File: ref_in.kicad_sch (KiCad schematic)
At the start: 15 parts, among them U1101 74LVC2GU04, U1102 74LVC2G04

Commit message: Update footprints: - SOD323F, SOD323, SOD123W... intead of generic handsolder version - 3225 xtal - use handsolder footprint - do not use handsolder version for ferrite beads - use SOT-23-6 instead of TSOP-6
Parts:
- D1102, D1103: footprint Diode_SMD:D_SOD-323_HandSoldering -> Diode_SMD:D_SOD-323F
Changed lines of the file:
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@@
       (effects (font (size 1.27 1.27)) (justify left))
     )
-    (property "Footprint" "Diode_SMD:D_SOD-323_HandSoldering" (id 2) (at 126.365 96.52 0)
+    (property "Footprint" "Diode_SMD:D_SOD-323F" (id 2) (at 126.365 96.52 0)
       (effects (font (size 1.27 1.27)) hide)
     )
@@
       (effects (font (size 1.27 1.27)) (justify left))
     )
-    (property "Footprint" "Diode_SMD:D_SOD-323_HandSoldering" (id 2) (at 125.095 106.68 0)
-      (effects (font (size 1.27 1.27)) hide)
-    )
+    (property "Footprint" "Diode_SMD:D_SOD-323F" (id 2) (at 125.095 106.68 0)
+      (effects (font (size 1.27 1.27)) hide)
+    )

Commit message: 74lvc2g04: swap units
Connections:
- net OUT: now also U1102.6; no longer U1102.4
- net at U1101.4: now also U1102.3; no longer U1102.1
- new net: U1102.1, U1102.4
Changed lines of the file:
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@@
     (pin "2")
   )
-  (symbol (lib_id "symbols:74LVC2G04") (at 189.23 101.6 0) (unit 1)
+  (symbol (lib_id "symbols:74LVC2G04") (at 189.23 101.6 0) (unit 2)
     (in_bom yes) (on_board yes) (fields_autoplaced)
     (property "Reference" "U1102" (id 0) (at 191.0715 94.0902 0))
@@
     (pin "5")
   )
-  (symbol (lib_id "symbols:74LVC2G04") (at 205.74 101.6 0) (unit 2)
+  (symbol (lib_id "symbols:74LVC2G04") (at 205.74 101.6 0) (unit 1)
     (in_bom yes) (on_board yes) (fields_autoplaced)
     (property "Reference" "U1102" (id 0) (at 207.5815 94.0902 0))

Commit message: Reconnect some things to simplify PCB routing
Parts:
- U1101: value 74LVC2GU04 -> (none); footprint Package_TO_SOT_SMD:SOT-23-6 -> (none)
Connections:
- net IN: now also C1102.1, JP1101.1 (A); no longer R1102.2
- net at D1102.1 (K), D1103.2 (A), R1103.1: now also R1102.1, U1101.3; no longer C1102.2, JP1101.2 (B), U1101.1
- net at U1102.3: now also U1101.6; no longer U1101.4
- new net: C1102.2, JP1101.2 (B), R1102.2
- new net: R1104.1, U1101.1, U1101.4
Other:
- moved on the sheet: C1102, JP1101, R1102
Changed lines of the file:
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@@
   (junction (at 147.32 113.03) (diameter 0) (color 0 0 0 0)
   )
+  (junction (at 129.54 101.6) (diameter 0) (color 0 0 0 0)
+  )
   (junction (at 203.2 60.96) (diameter 0) (color 0 0 0 0)
   )
-  (junction (at 129.54 101.6) (diameter 0) (color 0 0 0 0)
-  )
   (junction (at 73.66 101.6) (diameter 0) (color 0 0 0 0)
   )
@@
   (junction (at 165.1 50.8) (diameter 0) (color 0 0 0 0)
   )
+  (junction (at 111.76 101.6) (diameter 0) (color 0 0 0 0)
+  )
   (junction (at 165.1 60.96) (diameter 0) (color 0 0 0 0)
   )
-  (junction (at 110.49 101.6) (diameter 0) (color 0 0 0 0)
+  (junction (at 99.06 101.6) (diameter 0) (color 0 0 0 0)
   )
   (junction (at 203.2 50.8) (diameter 0) (color 0 0 0 0)
@@
   (junction (at 147.32 101.6) (diameter 0) (color 0 0 0 0)
   )
-  (junction (at 123.19 101.6) (diameter 0) (color 0 0 0 0)
-  )
   (junction (at 184.15 50.8) (diameter 0) (color 0 0 0 0)
   )
@@
     (stroke (width 0) (type default) (color 0 0 0 0))
   )
-  (wire (pts (xy 123.19 101.6) (xy 129.54 101.6))
-    (stroke (width 0) (type default) (color 0 0 0 0))
-  )
   (wire (pts (xy 215.9 60.96) (xy 203.2 60.96))
     (stroke (width 0) (type default) (color 0 0 0 0))
@@
     (stroke (width 0) (type default) (color 0 0 0 0))
   )
-  (wire (pts (xy 123.19 91.44) (xy 123.19 101.6))
+  (wire (pts (xy 111.76 91.44) (xy 111.76 101.6))
     (stroke (width 0) (type default) (color 0 0 0 0))
   )
@@
     (stroke (width 0) (type default) (color 0 0 0 0))
   )
-  (wire (pts (xy 106.68 101.6) (xy 110.49 101.6))
-    (stroke (width 0) (type default) (color 0 0 0 0))
-  )
   (wire (pts (xy 147.32 110.49) (xy 147.32 113.03))
     (stroke (width 0) (type default) (color 0 0 0 0))
   )
-  (wire (pts (xy 110.49 101.6) (xy 113.03 101.6))
+  (wire (pts (xy 99.06 101.6) (xy 101.6 101.6))
     (stroke (width 0) (type default) (color 0 0 0 0))
   )
@@
     (stroke (width 0) (type default) (color 0 0 0 0))
   )
+  (wire (pts (xy 124.46 101.6) (xy 129.54 101.6))
+    (stroke (width 0) (type default) (color 0 0 0 0))
+  )
+  (wire (pts (xy 111.76 101.6) (xy 116.84 101.6))
+    (stroke (width 0) (type default) (color 0 0 0 0))
+  )
   (wire (pts (xy 184.15 60.96) (xy 165.1 60.96))
     (stroke (width 0) (type default) (color 0 0 0 0))
   )
-  (wire (pts (xy 110.49 91.44) (xy 110.49 101.6))
+  (wire (pts (xy 99.06 91.44) (xy 99.06 101.6))
     (stroke (width 0) (type default) (color 0 0 0 0))
   )
@@
     (stroke (width 0) (type default) (color 0 0 0 0))
   )
-  (wire (pts (xy 121.92 91.44) (xy 123.19 91.44))
+  (wire (pts (xy 110.49 91.44) (xy 111.76 91.44))
     (stroke (width 0) (type default) (color 0 0 0 0))
   )
@@
     (stroke (width 0) (type default) (color 0 0 0 0))
   )
-  (wire (pts (xy 111.76 91.44) (xy 110.49 91.44))
-    (stroke (width 0) (type default) (color 0 0 0 0))
-  )
-  (wire (pts (xy 120.65 101.6) (xy 123.19 101.6))
+  (wire (pts (xy 100.33 91.44) (xy 99.06 91.44))
+    (stroke (width 0) (type default) (color 0 0 0 0))
+  )
+  (wire (pts (xy 109.22 101.6) (xy 111.76 101.6))
     (stroke (width 0) (type default) (color 0 0 0 0))
   )
@@
     (pin "3")
   )
-  (symbol (lib_id "Device:C") (at 116.84 101.6 90) (unit 1)
-    (in_bom yes) (on_board yes) (fields_autoplaced)
-    (property "Reference" "C1102" (id 0) (at 116.84 105.7894 90))
-    (property "Value" "10n" (id 1) (at 116.84 108.3263 90))
-    (property "Footprint" "Capacitor_SMD:C_0805_2012Metric" (id 2) (at 120.65 100.6348 0)
-      (effects (font (size 1.27 1.27)) hide)
-    )
-    (property "Datasheet" "~" (id 3) (at 116.84 101.6 0)
-      (effects (font (size 1.27 1.27)) hide)
-    )
-    (property "Spec1" "" (id 4) (at 116.84 110.8632 90))
-    (property "Spec2" "C0G" (id 5) (at 116.84 110.8632 90))
-    (property "Tolerance" "" (id 6) (at 116.84 115.937 90))
-    (property "Mfr" "Murata" (id 7) (at 116.84 101.6 0)
-      (effects (font (size 1.27 1.27)) hide)
-    )
-    (property "Mfr PN" "GRM2165C2A103JA01" (id 8) (at 116.84 101.6 0)
+  (symbol (lib_id "Device:C") (at 105.41 101.6 90) (unit 1)
+    (in_bom yes) (on_board yes) (fields_autoplaced)
+    (property "Reference" "C1102" (id 0) (at 105.41 105.7894 90))
+    (property "Value" "10n" (id 1) (at 105.41 108.3263 90))
+    (property "Footprint" "Capacitor_SMD:C_0805_2012Metric" (id 2) (at 109.22 100.6348 0)
+      (effects (font (size 1.27 1.27)) hide)
+    )
+    (property "Datasheet" "~" (id 3) (at 105.41 101.6 0)
+      (effects (font (size 1.27 1.27)) hide)
+    )
+    (property "Spec1" "" (id 4) (at 105.41 110.8632 90))
+    (property "Spec2" "C0G" (id 5) (at 105.41 110.8632 90))
+    (property "Tolerance" "" (id 6) (at 105.41 115.937 90))
+    (property "Mfr" "Murata" (id 7) (at 105.41 101.6 0)
+      (effects (font (size 1.27 1.27)) hide)
+    )
+    (property "Mfr PN" "GRM2165C2A103JA01" (id 8) (at 105.41 101.6 0)
       (effects (font (size 1.27 1.27)) hide)
     )
@@
     (pin "1")
   )
-  (symbol (lib_id "Jumper:Jumper_2_Open") (at 116.84 91.44 0) (unit 1)
-    (in_bom yes) (on_board yes) (fields_autoplaced)
-    (property "Reference" "JP1101" (id 0) (at 116.84 86.0892 0))
-    (property "Value" "DC" (id 1) (at 116.84 88.6261 0))
-    (property "Footprint" "Connector_PinHeader_2.54mm:PinHeader_1x02_P2.54mm_Vertical" (id 2) (at 116.84 91.44 0)
-      (effects (font (size 1.27 1.27)) hide)
-    )
-    (property "Datasheet" "~" (id 3) (at 116.84 91.44 0)
+  (symbol (lib_id "Jumper:Jumper_2_Open") (at 105.41 91.44 0) (unit 1)
+    (in_bom yes) (on_board yes) (fields_autoplaced)
+    (property "Reference" "JP1101" (id 0) (at 105.41 86.0892 0))
+    (property "Value" "DC" (id 1) (at 105.41 88.6261 0))
+    (property "Footprint" "Connector_PinHeader_2.54mm:PinHeader_1x02_P2.54mm_Vertical" (id 2) (at 105.41 91.44 0)
+      (effects (font (size 1.27 1.27)) hide)
+    )
+    (property "Datasheet" "~" (id 3) (at 105.41 91.44 0)
       (effects (font (size 1.27 1.27)) hide)
     )
@@
     (pin "2")
   )
-  (symbol (lib_id "symbols:74LVC2GU04") (at 172.72 101.6 0) (unit 2)
+  (symbol (lib_id "symbols:74LVC2GU04") (at 172.72 101.6 0) (unit 1)
     (in_bom yes) (on_board yes) (fields_autoplaced)
     (property "Reference" "U1101" (id 0) (at 174.5615 94.0902 0))
-    (property "Value" "74LVC2GU04" (id 1) (at 174.5615 96.6271 0))
-    (property "Footprint" "Package_TO_SOT_SMD:SOT-23-6" (id 2) (at 172.72 83.82 0)
+    (property "Value" "" (id 1) (at 174.5615 96.6271 0))
+    (property "Footprint" "" (id 2) (at 172.72 83.82 0)
       (effects (font (size 1.27 1.27)) hide)
     )
@@
       (effects (font (size 1.27 1.27)) (justify left))
     )
-    (property "Value" "74LVC2GU04" (id 1) (at 186.3713 57.5822 0)
-      (effects (font (size 1.27 1.27)) (justify left))
-    )
-    (property "Footprint" "Package_TO_SOT_SMD:SOT-23-6" (id 2) (at 184.15 38.1 0)
+    (property "Value" "" (id 1) (at 186.3713 57.5822 0)
+      (effects (font (size 1.27 1.27)) (justify left))
+    )
+    (property "Footprint" "" (id 2) (at 184.15 38.1 0)
       (effects (font (size 1.27 1.27)) hide)
     )
@@
     (pin "2")
   )
-  (symbol (lib_id "Device:R") (at 102.87 101.6 270) (unit 1)
-    (in_bom yes) (on_board yes) (fields_autoplaced)
-    (property "Reference" "R1102" (id 0) (at 102.87 96.8842 90))
-    (property "Value" "1k" (id 1) (at 102.87 99.4211 90))
-    (property "Footprint" "Resistor_SMD:R_0805_2012Metric" (id 2) (at 102.87 99.822 90)
-      (effects (font (size 1.27 1.27)) hide)
-    )
-    (property "Datasheet" "~" (id 3) (at 102.87 101.6 0)
-      (effects (font (size 1.27 1.27)) hide)
-    )
-    (property "Tolerance" "" (id 4) (at 102.87 101.6 0)
-      (effects (font (size 1.27 1.27)) hide)
-    )
-    (property "Mfr" "Bourns" (id 5) (at 102.87 101.6 0)
-      (effects (font (size 1.27 1.27)) hide)
-    )
-    (property "Mfr PN" "CR0805-FX-1001ELF" (id 6) (at 102.87 101.6 0)
-      (effects (font (size 1.27 1.27)) hide)
-    )
-    (pin "1")
-    (pin "2")
-  )
-  (symbol (lib_id "symbols:74LVC2GU04") (at 154.94 101.6 0) (unit 1)
+  (symbol (lib_id "Device:R") (at 120.65 101.6 270) (unit 1)
+    (in_bom yes) (on_board yes) (fields_autoplaced)
+    (property "Reference" "R1102" (id 0) (at 120.65 96.8842 90))
+    (property "Value" "1k" (id 1) (at 120.65 99.4211 90))
+    (property "Footprint" "Resistor_SMD:R_0805_2012Metric" (id 2) (at 120.65 99.822 90)
+      (effects (font (size 1.27 1.27)) hide)
+    )
+    (property "Datasheet" "~" (id 3) (at 120.65 101.6 0)
+      (effects (font (size 1.27 1.27)) hide)
+    )
+    (property "Tolerance" "" (id 4) (at 120.65 101.6 0)
+      (effects (font (size 1.27 1.27)) hide)
+    )
+    (property "Mfr" "Bourns" (id 5) (at 120.65 101.6 0)
+      (effects (font (size 1.27 1.27)) hide)
+    )
+    (property "Mfr PN" "CR0805-FX-1001ELF" (id 6) (at 120.65 101.6 0)
+      (effects (font (size 1.27 1.27)) hide)
+    )
+    (pin "1")
+    (pin "2")
+  )
+  (symbol (lib_id "symbols:74LVC2GU04") (at 154.94 101.6 0) (unit 2)
     (in_bom yes) (on_board yes) (fields_autoplaced)
     (property "Reference" "U1101" (id 0) (at 156.7815 94.0902 0))
-    (property "Value" "74LVC2GU04" (id 1) (at 156.7815 96.6271 0))
-    (property "Footprint" "Package_TO_SOT_SMD:SOT-23-6" (id 2) (at 154.94 83.82 0)
-      (effects (font (size 1.27 1.27)) hide)
-    )
+    (property "Value" "" (id 1) (at 156.7815 96.6271 0))
+    (property "Footprint" "" (id 2) (at 154.94 83.82 0)
+      (effects (font (size 1.27 1.27)) hide)
+    )

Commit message: Fix footprints, values and PNs
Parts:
- U1101: value (none) -> 74LVC2GU04; footprint (none) -> Package_TO_SOT_SMD:SOT-23-6
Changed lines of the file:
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@@
     (in_bom yes) (on_board yes) (fields_autoplaced)
     (property "Reference" "U1101" (id 0) (at 174.5615 94.0902 0))
-    (property "Value" "" (id 1) (at 174.5615 96.6271 0))
-    (property "Footprint" "" (id 2) (at 172.72 83.82 0)
+    (property "Value" "74LVC2GU04" (id 1) (at 174.5615 96.6271 0))
+    (property "Footprint" "Package_TO_SOT_SMD:SOT-23-6" (id 2) (at 172.72 83.82 0)
       (effects (font (size 1.27 1.27)) hide)
     )
@@
       (effects (font (size 1.27 1.27)) (justify left))
     )
-    (property "Value" "" (id 1) (at 186.3713 57.5822 0)
-      (effects (font (size 1.27 1.27)) (justify left))
-    )
-    (property "Footprint" "" (id 2) (at 184.15 38.1 0)
+    (property "Value" "74LVC2GU04" (id 1) (at 186.3713 57.5822 0)
+      (effects (font (size 1.27 1.27)) (justify left))
+    )
+    (property "Footprint" "Package_TO_SOT_SMD:SOT-23-6" (id 2) (at 184.15 38.1 0)
       (effects (font (size 1.27 1.27)) hide)
     )
@@
     (in_bom yes) (on_board yes) (fields_autoplaced)
     (property "Reference" "U1101" (id 0) (at 156.7815 94.0902 0))
-    (property "Value" "" (id 1) (at 156.7815 96.6271 0))
-    (property "Footprint" "" (id 2) (at 154.94 83.82 0)
-      (effects (font (size 1.27 1.27)) hide)
-    )
+    (property "Value" "74LVC2GU04" (id 1) (at 156.7815 96.6271 0))
+    (property "Footprint" "Package_TO_SOT_SMD:SOT-23-6" (id 2) (at 154.94 83.82 0)
+      (effects (font (size 1.27 1.27)) hide)
+    )

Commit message: VCXO, REF_IN: add reflection damping resistors
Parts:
- added R1105: 49.9, Resistor_SMD:R_0805_2012Metric, symbol Device:R
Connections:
- net OUT: now also R1105.2; no longer U1102.6
- new net: R1105.1, U1102.6
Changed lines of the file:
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@@
     (stroke (width 0) (type default) (color 0 0 0 0))
   )
-  (wire (pts (xy 213.36 101.6) (xy 218.44 101.6))
+  (wire (pts (xy 213.36 101.6) (xy 217.17 101.6))
     (stroke (width 0) (type default) (color 0 0 0 0))
   )
@@
     (stroke (width 0) (type default) (color 0 0 0 0))
   )
+  (wire (pts (xy 224.79 101.6) (xy 228.6 101.6))
+    (stroke (width 0) (type default) (color 0 0 0 0))
+  )
   (wire (pts (xy 203.2 50.8) (xy 203.2 52.07))
     (stroke (width 0) (type default) (color 0 0 0 0))
@@
     (stroke (width 0) (type default) (color 0 0 0 0))
   )
-  (hierarchical_label "OUT" (shape output) (at 218.44 101.6 0)
+  (hierarchical_label "OUT" (shape output) (at 228.6 101.6 0)
     (effects (font (size 1.27 1.27)) (justify left))
   )
@@
       (effects (font (size 1.27 1.27)) hide)
     )
+    (pin "1")
+    (pin "2")
+  )
+  (symbol (lib_id "Device:R") (at 220.98 101.6 90) (unit 1)
+    (in_bom yes) (on_board yes) (fields_autoplaced)
+    (property "Reference" "R1105" (id 0) (at 220.98 96.8842 90))
+    (property "Value" "49.9" (id 1) (at 220.98 99.4211 90))
+    (property "Footprint" "Resistor_SMD:R_0805_2012Metric" (id 2) (at 220.98 103.378 90)
+      (effects (font (size 1.27 1.27)) hide)
+    )
+    (property "Datasheet" "~" (id 3) (at 220.98 101.6 0)
+      (effects (font (size 1.27 1.27)) hide)
+    )
+    (property "Mfr" "Bourns" (id 4) (at 220.98 101.6 0)
+      (effects (font (size 1.27 1.27)) hide)
+    )
+    (property "Mfr PN" "CR0805-FX-49R9ELF" (id 5) (at 220.98 101.6 0)
+      (effects (font (size 1.27 1.27)) hide)
+    )

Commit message: PCB: WIP Schematic: minor changes (decoupling, logic element ordering)
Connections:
- net at D1102.1 (K), D1103.2 (A), R1102.1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: now also U1101.1; no longer U1101.3
- net at R1105.1: now also U1102.4; no longer U1102.6
- net at U1101.6: now also R1104.1, U1101.3; no longer U1102.3
- net at U1102.1: now also U1101.4; no longer U1102.4
- new net: U1102.3, U1102.6
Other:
- moved on the sheet: U1101A, U1101B, U1102A, U1102B

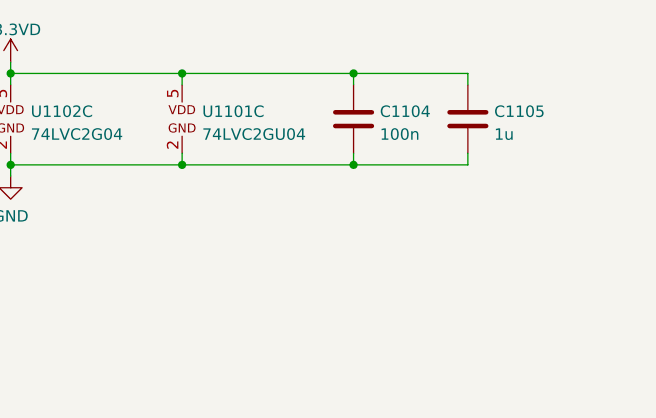
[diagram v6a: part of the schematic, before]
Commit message: Update schematic: - Redesign of decoupling based on swcad modelling (predominantly use 1uf, no paralleled caps) - Reroute REF_CLK_IN, CLK_SEL net to different FPGA pins - Some net renaming - Ext conn: add decoupling to 3v3 output - Reassign references to all components PCB: routing almost finished
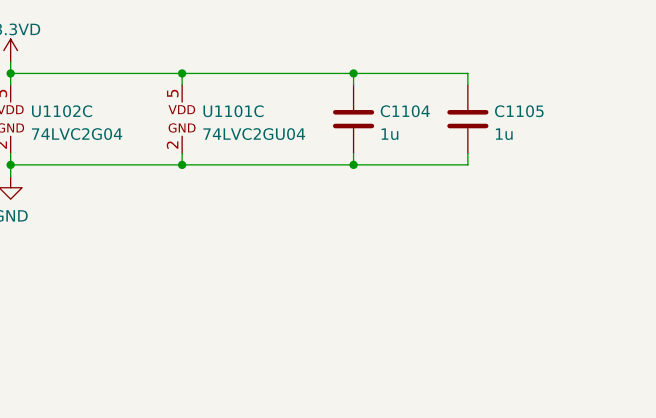
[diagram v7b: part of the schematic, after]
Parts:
- C1104: value 100n -> 1u; Mfr PN CL21B104KBFNNNE -> CL21B105KOFNNNG
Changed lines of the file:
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@@
-    (pin "2")
-  )
-  (symbol (lib_id "Device:C") (at 203.2 55.88 180) (unit 1)
-    (in_bom yes) (on_board yes) (fields_autoplaced)
-    (property "Reference" "C1104" (id 0) (at 206.121 55.0453 0)
-      (effects (font (size 1.27 1.27)) (justify right))
-    )
-    (property "Value" "100n" (id 1) (at 206.121 57.5822 0)
-      (effects (font (size 1.27 1.27)) (justify right))
-    )
-    (property "Footprint" "Capacitor_SMD:C_0805_2012Metric" (id 2) (at 202.2348 52.07 0)
-      (effects (font (size 1.27 1.27)) hide)
-    )
-    (property "Datasheet" "~" (id 3) (at 203.2 55.88 0)
-      (effects (font (size 1.27 1.27)) hide)
-    )
-    (property "Spec1" "" (id 4) (at 203.2 55.88 0)
-      (effects (font (size 1.27 1.27)) hide)
-    )
-    (property "Spec2" "" (id 5) (at 203.2 55.88 0)
-      (effects (font (size 1.27 1.27)) hide)
-    )
-    (property "Tolerance" "" (id 6) (at 203.2 55.88 0)
-      (effects (font (size 1.27 1.27)) hide)
-    )
-    (property "Mfr" "Samsung" (id 7) (at 203.2 55.88 0)
-      (effects (font (size 1.27 1.27)) hide)
-    )
-    (property "Mfr PN" "CL21B104KBFNNNE" (id 8) (at 203.2 55.88 0)
-      (effects (font (size 1.27 1.27)) hide)
-    )
-    (pin "1")
     (pin "2")
   )
@@
       (effects (font (size 1.27 1.27)) hide)
     )
+    (pin "1")
+    (pin "2")
+  )
+  (symbol (lib_id "Device:C") (at 203.2 55.88 180) (unit 1)
+    (in_bom yes) (on_board yes) (fields_autoplaced)
+    (property "Reference" "C1104" (id 0) (at 206.121 55.0453 0)
+      (effects (font (size 1.27 1.27)) (justify right))
+    )
+    (property "Value" "1u" (id 1) (at 206.121 57.5822 0)
+      (effects (font (size 1.27 1.27)) (justify right))
+    )
+    (property "Footprint" "Capacitor_SMD:C_0805_2012Metric" (id 2) (at 202.2348 52.07 0)
+      (effects (font (size 1.27 1.27)) hide)
+    )
+    (property "Datasheet" "~" (id 3) (at 203.2 55.88 0)
+      (effects (font (size 1.27 1.27)) hide)
+    )
+    (property "Spec1" "" (id 4) (at 203.2 55.88 0)
+      (effects (font (size 1.27 1.27)) hide)
+    )
+    (property "Spec2" "" (id 5) (at 203.2 55.88 0)
+      (effects (font (size 1.27 1.27)) hide)
+    )
+    (property "Tolerance" "" (id 6) (at 203.2 55.88 0)
+      (effects (font (size 1.27 1.27)) hide)
+    )
+    (property "Mfr" "Samsung" (id 7) (at 203.2 55.88 0)
+      (effects (font (size 1.27 1.27)) hide)
+    )
+    (property "Mfr PN" "CL21B105KOFNNNG" (id 8) (at 203.2 55.88 0)
+      (effects (font (size 1.27 1.27)) hide)
+    )

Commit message: - Add matching / anti-ring resistors to clock nets - Use 0603 resistors for anti-ring - Improve CLK_OUT routing
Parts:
- R1105: footprint Resistor_SMD:R_0805_2012Metric -> Resistor_SMD:R_0603_1608Metric; Mfr PN CR0805-FX-49R9ELF -> CR0603-FX-49R9ELF
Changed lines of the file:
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@@
     (property "Reference" "R1105" (id 0) (at 220.98 96.8842 90))
     (property "Value" "49.9" (id 1) (at 220.98 99.4211 90))
-    (property "Footprint" "Resistor_SMD:R_0805_2012Metric" (id 2) (at 220.98 103.378 90)
+    (property "Footprint" "Resistor_SMD:R_0603_1608Metric" (id 2) (at 220.98 103.378 90)
       (effects (font (size 1.27 1.27)) hide)
     )
@@
       (effects (font (size 1.27 1.27)) hide)
     )
-    (property "Mfr PN" "CR0805-FX-49R9ELF" (id 5) (at 220.98 101.6 0)
+    (property "Mfr PN" "CR0603-FX-49R9ELF" (id 5) (at 220.98 101.6 0)
       (effects (font (size 1.27 1.27)) hide)
     )
